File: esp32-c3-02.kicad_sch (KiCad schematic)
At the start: 0 parts

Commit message: feat: add sensor and user interface schematic sheets, update ESP32 sheet
- Added Sensors schematic sheet for integrating all sensor-related components.
- Added User Interface sheet to host user-interaction components (e.g., buttons, displays).
- Populated the ESP32 sheet with the following sections:
    - USB-to-UART Connector
    - ESP32 Module
    - Flash Memory
    - SD Card Module
- Each section is modular and self-contained, designed for clarity and easy testing.
- Enabled signal access (e.g., USB_D+, USB_D-, VBUS) in the USB-to-UART section via hierarchical labels from the parent sheet.
- Added test points on SPI lines within the ESP32 sheet to facilitate hardware debugging and validation.
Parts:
- added C10, C13, C14, C8: 0u1, symbol Device:C
- added C11, C12: 10u, symbol Device:C_Polarized
- added C7: 1u, symbol Device:C
- added C9: 4u7, symbol Device:C_Polarized
- added J3: GSD090012SEU, GSD090012SEU:AMPHENOL_GSD090012SEU, symbol GSD090012SEU:GSD090012SEU
- added LED5: LTST-C170GKT, LEDC2012X120N, symbol LTST-C170GKT:LTST-C170GKT
- added LED6: LTST-C170KRKT, LEDC2012X120N, symbol LTST-C170KRKT:LTST-C170KRKT
- added R11: 22k1, symbol Device:R
- added R12: 47k5, symbol Device:R
- added R13: 1k, symbol Device:R
- added R14, R15, R19, R20: 50, symbol Device:R
- added R16, R17: 470, symbol Device:R
- added R18: 10k, symbol Device:R
- added TP1: Test MOSI_DI, symbol Connector:TestPoint
- added TP2: Test MISO_DO, symbol Connector:TestPoint
- added TP3: Test SCLK, symbol Connector:TestPoint
- added TP4: Test CS_SD, symbol Connector:TestPoint
- added TP5: Test CS, symbol Connector:TestPoint
- added U3: ESP32-C3-WROOM-02-H4, ESP32-C3-WROOM-02-H4:MODULE_ESP32-C3-WROOM-02-H4, symbol ESP32-C3-WROOM-02-H4:ESP32-C3-WROOM-02-H4
- added U4: CP2102N-Axx-xQFN20, Package_DFN_QFN:SiliconLabs_QFN-20-1EP_3x3mm_P0.5mm, symbol Interface_USB:CP2102N-Axx-xQFN20
- added U5: USBLC6-2SC6, Package_TO_SOT_SMD:SOT-23-6, symbol Power_Protection:USBLC6-2SC6
- added U6: W25Q32JVSSIQ, W25Q32JVSSIQ:SOIC127P790X216-8N, symbol W25Q32JVSSIQ:W25Q32JVSSIQ
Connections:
- new net: LED6.1 (K), R17.2
- new net: R14.2, U3.5 (IO6)
- new net: R15.1, U3.6 (IO7)
- new net: R20.2, U6.2 (DO(IO1))
- new net: R13.2, U4.9 (~{RST})
- new net: R17.1, U4.19 (~{RXT}/GPIO.3)
- new net: R16.1, U4.20 (~{TXT}/GPIO.2)
- new net: C7.1, R11.2, R12.1, U4.8 (VBUS)
- new net: J3.7 (DAT0), R19.1
- new net: LED5.1 (K), R16.2
- new net +3.3V: C10.1, C11.1, C12.1, C13.1, C14.1, C8.2, C9.1, J3.4 (VDD1), LED5.2 (A), LED6.2 (A), R13.1, R18.2, U3.1 (3V3), U4.6 (VDD), U4.7 (VREGIN), U6.3 (~{WP}(IO2)), U6.7 (~{HOLD}/~{RESET}(IO3)), U6.8 (VCC)
- new net BOOT: U3.8 (IO9)
- new net CS: TP5.1, U3.10 (IO10), U6.1 (~{CS})
- new net CS_SD: J3.1 (CD/DAT3), R18.1, TP4.1, U3.18 (IO0)
- new net CTS: U4.15 (~{CTS})
- new net EN: U3.2 (EN)
- new net GND: C10.2, C11.2, C12.2, C13.2, C14.2, C7.2, C8.1, C9.2, J3.3 (VSS1), J3.6 (VSS2), J3.8 (DAT1), J3.9 (DAT2), J3.G1 (SHIELD_GND), J3.G2 (SHIELD_GND), J3.G3 (SHIELD_GND), J3.G4 (SHIELD_GND), R12.2, U3.19 (GND), U3.20 (GND), U3.21 (GND), U3.22 (GND), U3.23 (GND), U3.24 (GND), U3.25 (GND), U3.26 (GND), U3.27 (GND), U3.28 (GND), U3.29 (GND), U3.30 (GND), U3.31 (GND), U3.32 (GND), U3.33 (GND), U3.34 (GND), U3.35 (GND), U3.36 (GND), U3.37 (GND), U3.38 (GND), U3.39 (GND), U3.9 (GND), U4.12 (GND), U4.21 (GND), U4.3 (GND), U5.2 (GND), U6.4 (GND)
- new net GPIO18: U3.13 (IO18)
- new net GPIO19: U3.14 (IO19)
- new net GPIO8: U3.7 (IO8)
- new net MIC_OUT: U3.4 (IO5)
- new net MISO_DO: R19.2, R20.1, TP2.1, U3.16 (IO2)
- new net MOSI_DI: J3.2 (CMD), R15.2, TP1.1, U6.5 (DI(IO0))
- new net PHOTO_SENSOR: U3.17 (IO1)
- new net RTS: U4.16 (~{RTS})
- new net RX_TX: U3.12 (TXD), U4.17 (RXD)
- new net SCL: U3.15 (IO3)
- new net SCLK: J3.5 (CLK), R14.1, TP3.1, U6.6 (CLK)
- new net SDA: U3.3 (IO4)
- new net TX_RX: U3.11 (RXD), U4.18 (TXD)
- new net USB_D+: U4.4 (D+), U5.3 (I/O2), U5.4 (I/O2)
- new net USB_D-: U4.5 (D-), U5.1 (I/O1), U5.6 (I/O1)
- new net VBUS: R11.1, U5.5 (VBUS)
- no-connect marks 0 -> 7
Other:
- added sheet Sensors (sensors.kicad_sch)
- added sheet User interface (user_interface.kicad_sch)
- note added: "Esp32 section"
- note added: "Flash memory"
- note added: "SD card module"
- note added: "Test points"
- note added: "USB to UART converter section"

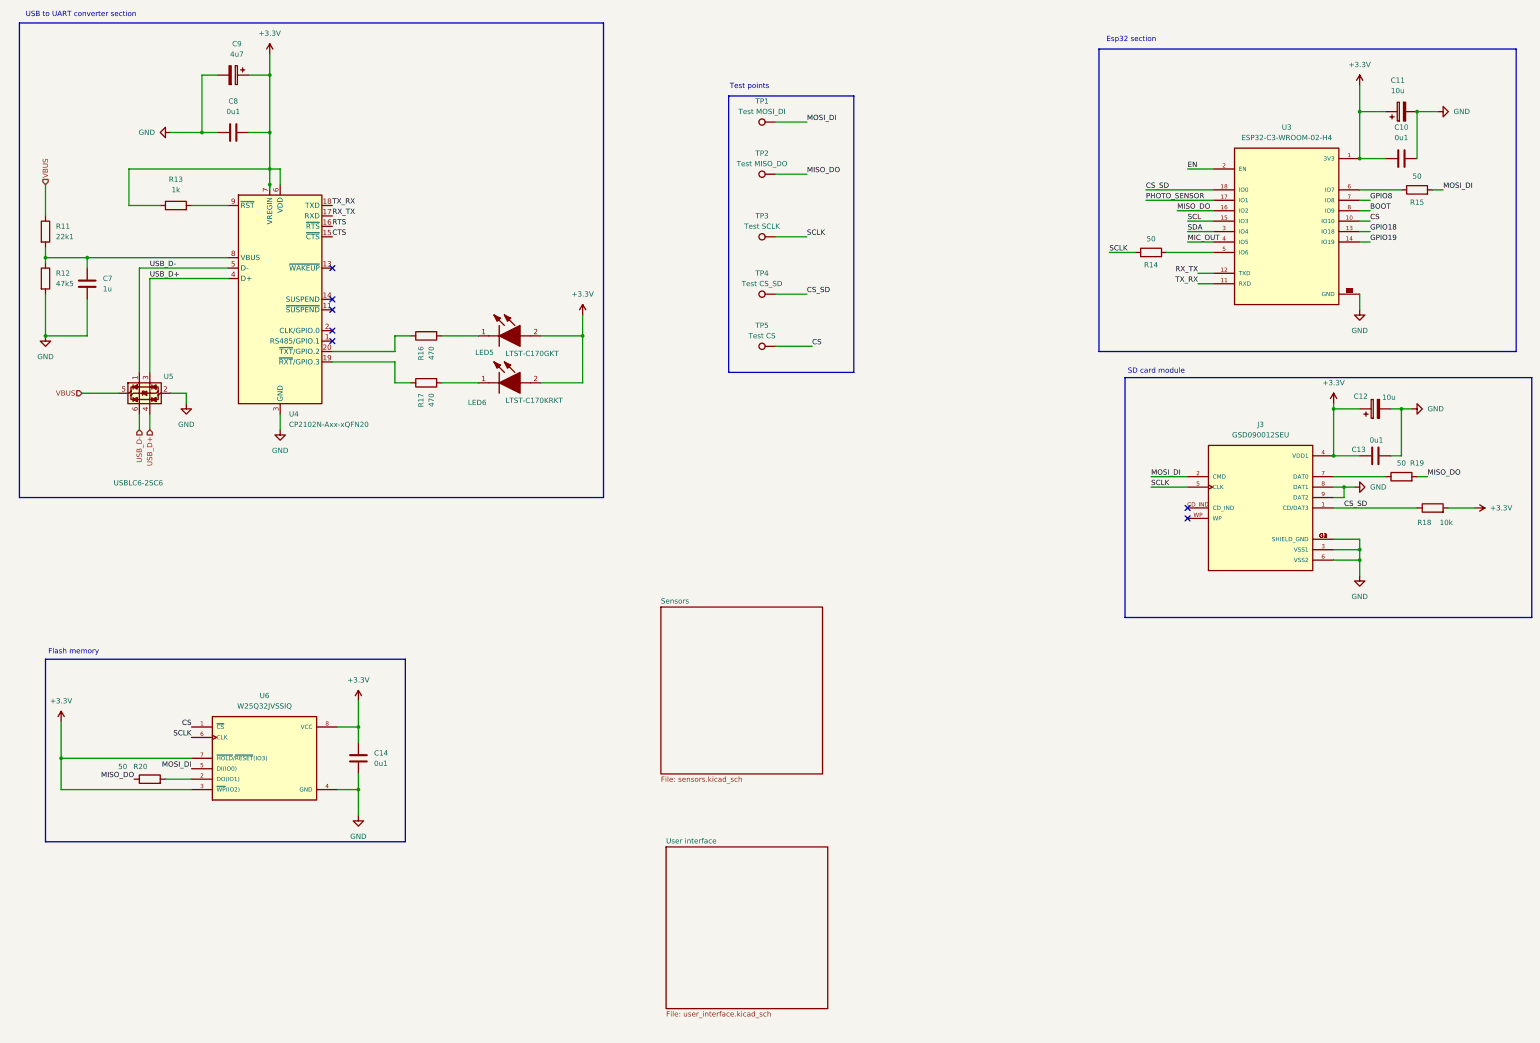
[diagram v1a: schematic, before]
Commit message: feat: populate sensor and user interface schematic sheets; assign footprints
- Populated the Sensors schematic sheet with the following components:
    - BME280: Temperature and humidity sensor
    - Photoresistor: For measuring ambient light levels
    - Sound Sensor Section: Includes a microphone and preamplifier to amplify audio signals for microcontroller processing

- Populated the User Interface schematic sheet with:
    - Boot and reset controls for the microcontroller
    - Breakout lines for external devices:
        - One for I²C-based peripherals (e.g., OLED display)
        - One for general-purpose I/O devices

- Both the Sensors and User Interface sheets access necessary pins (e.g., I²C, GPIO, control signals) from the parent ESP32
sheet using hierarchical labels, enabling clean and modular design.

- Assigned appropriate footprints to all components.
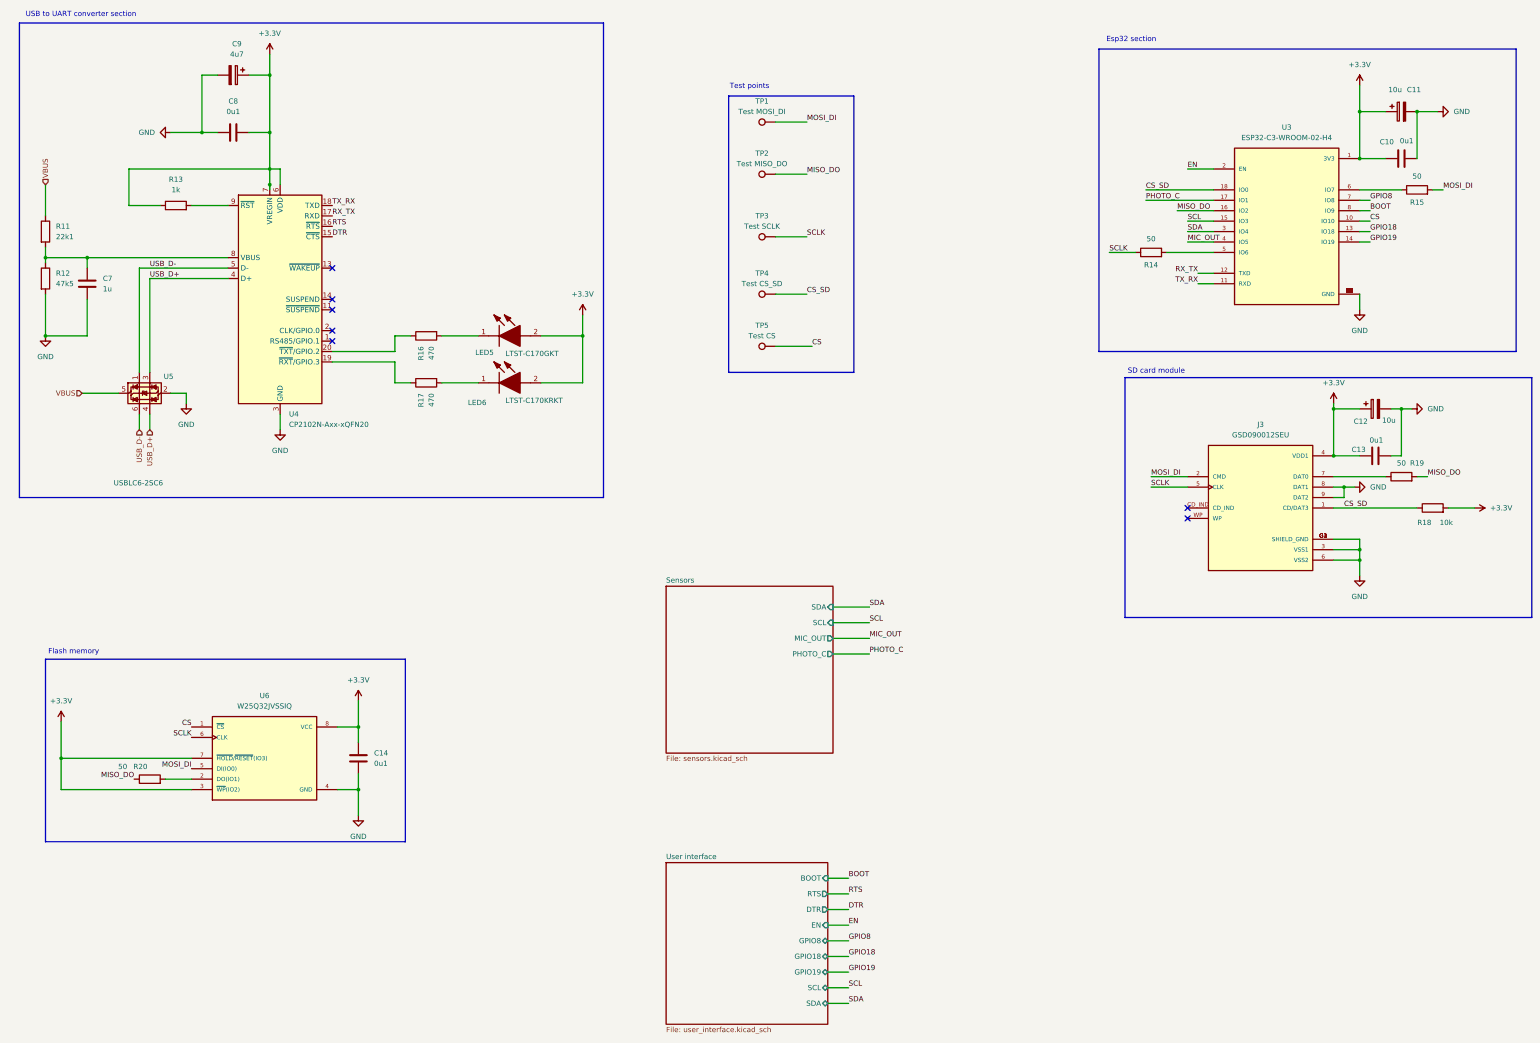
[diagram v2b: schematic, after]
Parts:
- C10, C13, C14, C7, C8: footprint (none) -> Capacitor_SMD:C_0805_2012Metric
- C11, C12, C9: footprint (none) -> ESP32 Project Footprints:T491A
- LED5, LED6: footprint LEDC2012X120N -> ESP32 Project Footprints:LEDC2012X120N
- R11, R12, R13, R14, R15, R16, R17, R18, R19, R20: footprint (none) -> Resistor_SMD:R_0805_2012Metric
- TP1, TP2, TP3, TP4, TP5: footprint (none) -> TestPoint:TestPoint_Pad_D1.0mm
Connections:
- net CTS renamed DTR
- net PHOTO_SENSOR renamed PHOTO_C
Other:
- sheet Sensors ports: added MIC_OUT, PHOTO_C, SCL, SDA; removed none
- sheet User interface ports: added BOOT, DTR, EN, GPIO18, GPIO19, GPIO8, RTS, SCL, SDA; removed none

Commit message: refactor: update label naming for net class scope resolution; set up PCB constraints
- Renamed schematic labels to follow a net class–based naming convention for
better scope resolution (e.g., labels in the SPI net class now use a SPI_ prefix).

- Configured the PCB stack-up to use a 4-layer board.

- Applied design constraints (e.g., trace width, spacing) based on the
PCB manufacturer's recommended specifications.
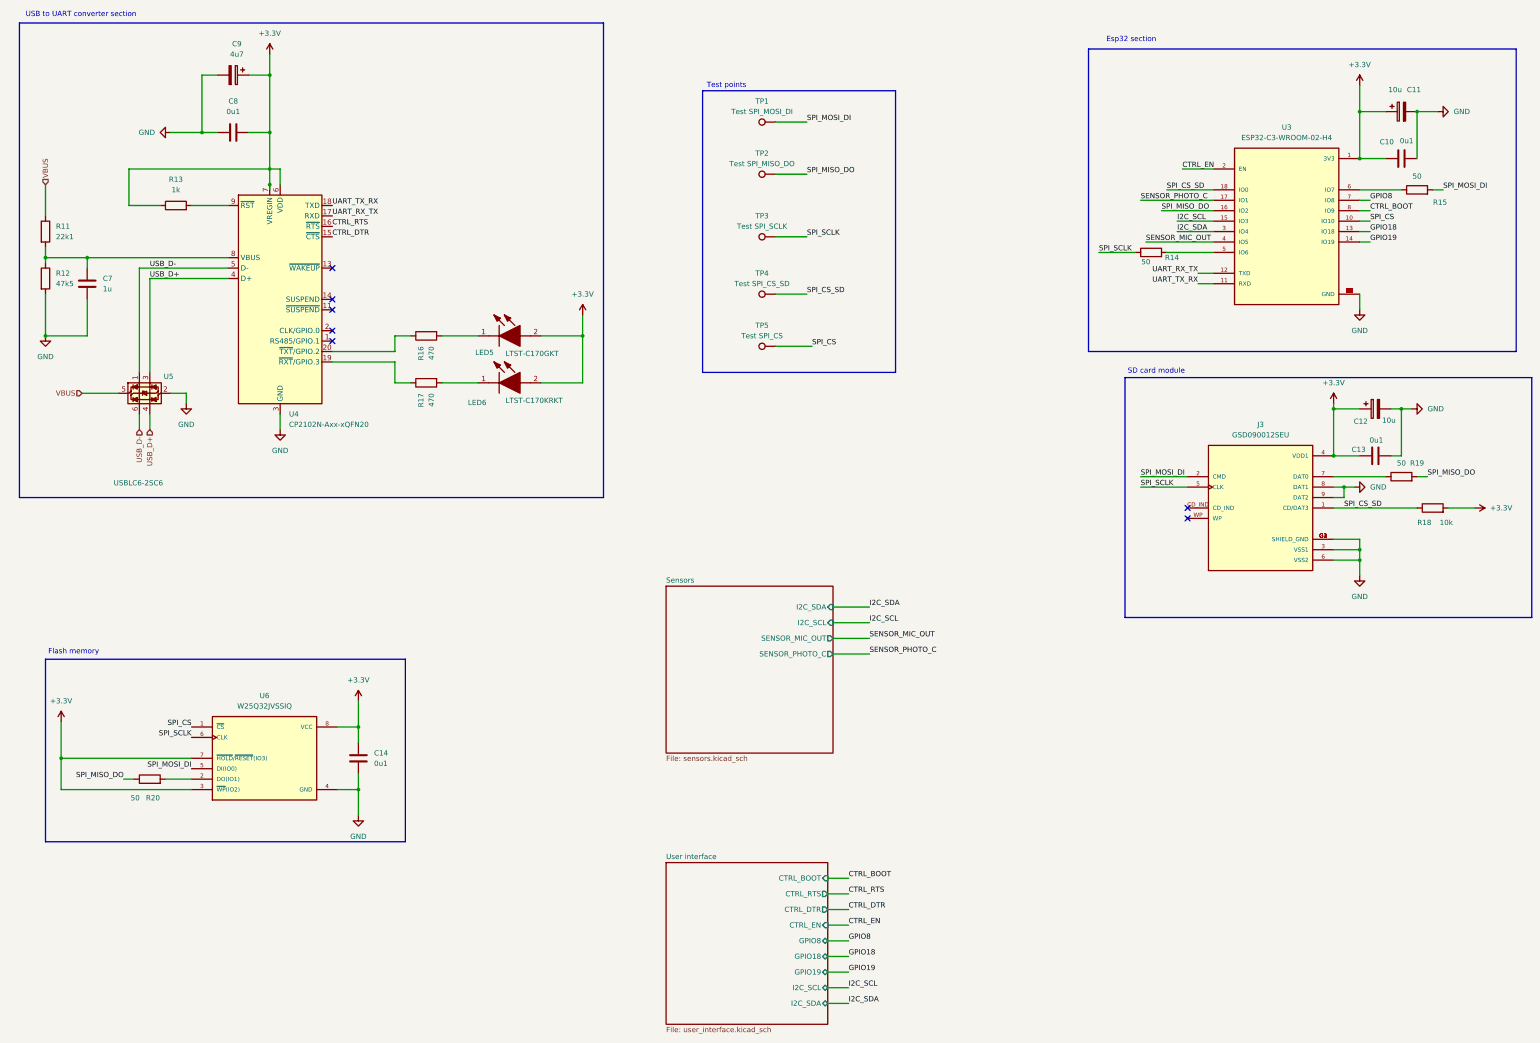
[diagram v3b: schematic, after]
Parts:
- TP1: value Test MOSI_DI -> Test SPI_MOSI_DI
- TP2: value Test MISO_DO -> Test SPI_MISO_DO
- TP3: value Test SCLK -> Test SPI_SCLK
- TP4: value Test CS_SD -> Test SPI_CS_SD
- TP5: value Test CS -> Test SPI_CS
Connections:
- net BOOT renamed CTRL_BOOT
- net CS renamed SPI_CS
- net CS_SD renamed SPI_CS_SD
- net DTR renamed CTRL_DTR
- net EN renamed CTRL_EN
- net MIC_OUT renamed SENSOR_MIC_OUT
- net MISO_DO renamed SPI_MISO_DO
- net MOSI_DI renamed SPI_MOSI_DI
- net PHOTO_C renamed SENSOR_PHOTO_C
- net RTS renamed CTRL_RTS
- net RX_TX renamed UART_RX_TX
- net SCL renamed I2C_SCL
- net SCLK renamed SPI_SCLK
- net SDA renamed I2C_SDA
- net TX_RX renamed UART_TX_RX
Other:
- sheet Sensors ports: added I2C_SCL, I2C_SDA, SENSOR_MIC_OUT, SENSOR_PHOTO_C; removed MIC_OUT, PHOTO_C, SCL, SDA
- sheet User interface ports: added CTRL_BOOT, CTRL_DTR, CTRL_EN, CTRL_RTS, I2C_SCL, I2C_SDA; removed BOOT, DTR, EN, RTS, SCL, SDA
